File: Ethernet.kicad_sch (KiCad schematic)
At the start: 22 parts, among them J1 PoE, J2301 X05ADGWA3DY1027, U2301 RCLAMP0524P, U2302 RCLAMP0524P

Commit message: Reannotate the board
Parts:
- renumbered C2301 to C71, C2302 to C72, C2303 to C73, C2304 to C74, C2305 to C75, C2306 to C76, C2307 to C77, C2308 to C78, C2309 to C79, D2301 to D20, D2302 to D21, J2301 to J19, J1 to J20, R2301 to R58, R2302 to R59, R2303 to R60, R2304 to R61, R2305 to R62, R2306 to R63, TR2301 to TR1, U2301 to U28, U2302 to U29
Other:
- moved on the sheet: C77

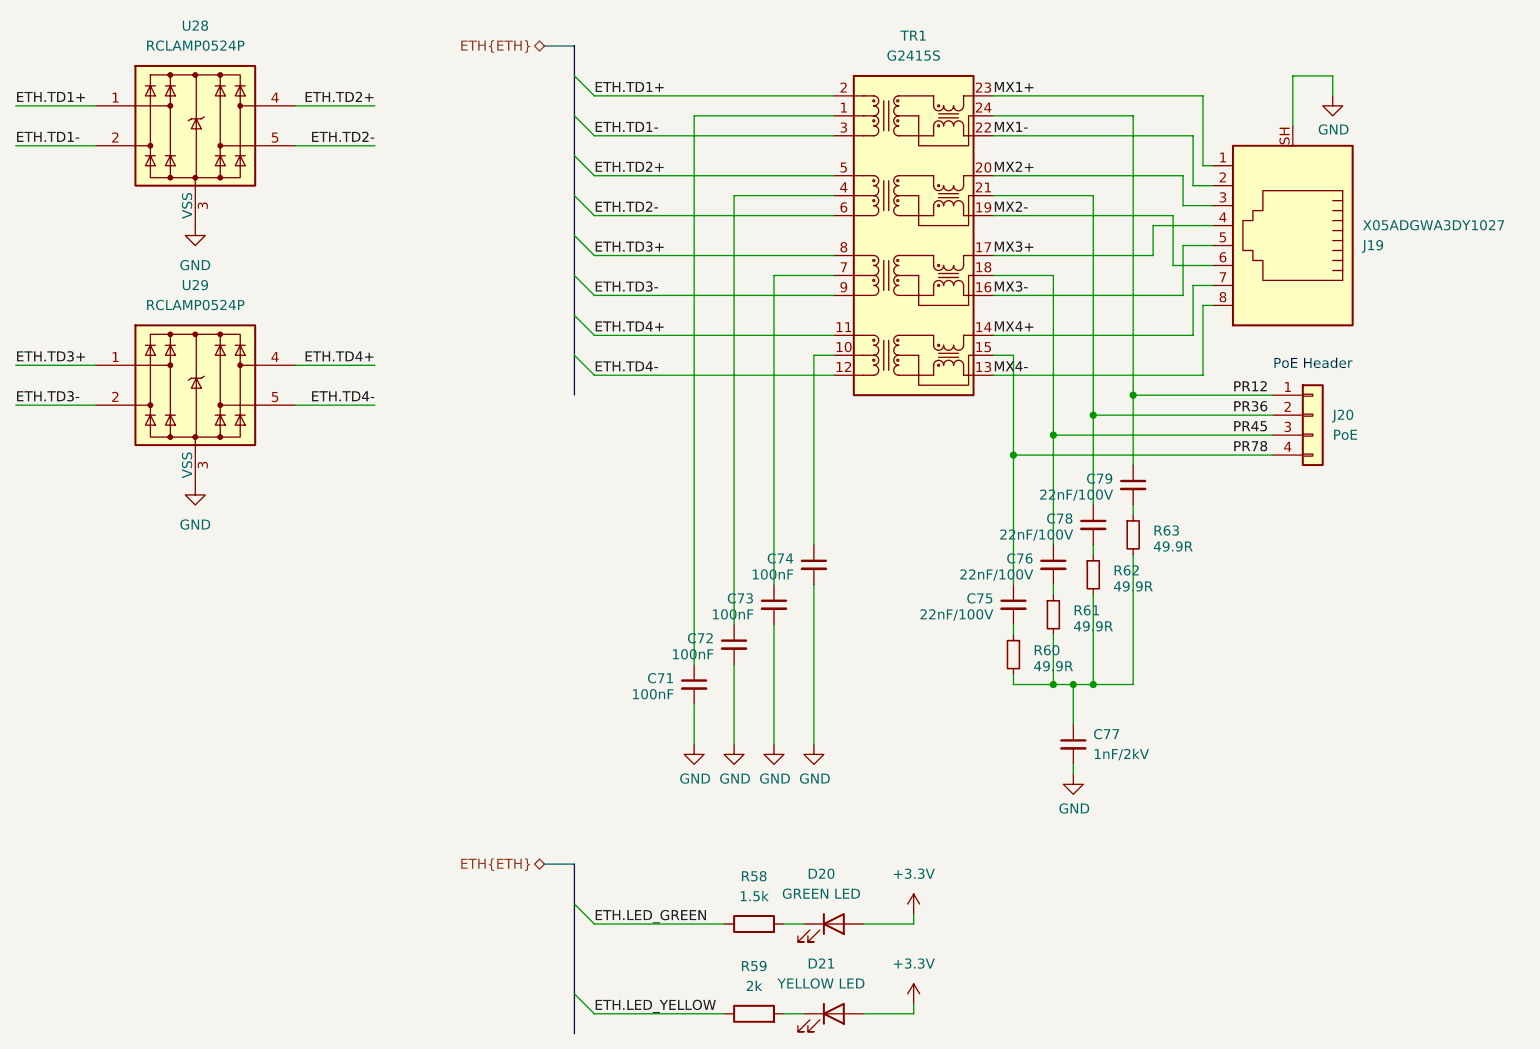
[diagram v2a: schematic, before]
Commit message: Add GND/3.3V/5V headers, add missing JLC part numbers
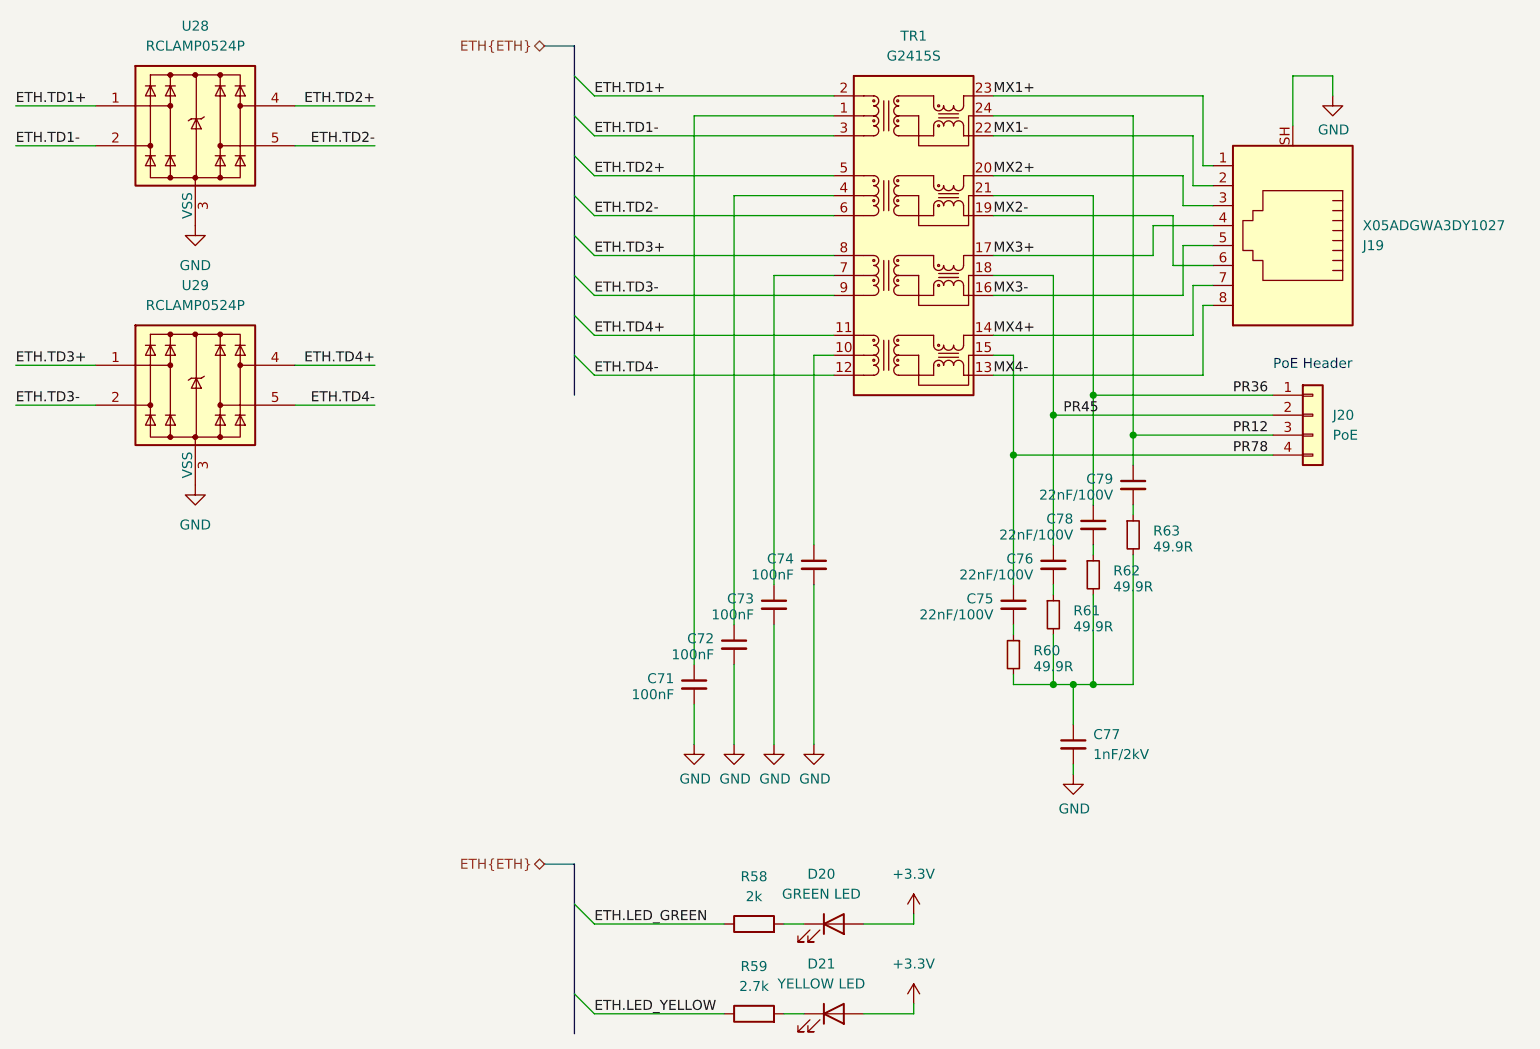
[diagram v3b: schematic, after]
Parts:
- J20: footprint Connector_PinSocket_2.54mm:PinSocket_1x04_P2.54mm_Vertical_SMD_Pin1Left -> Connector_PinSocket_2.54mm:PinSocket_2x02_P2.54mm_Vertical_SMD; LCSC (none) -> C5160817
- R58: value 1.5k -> 2k; footprint Resistor_SMD:R_0402_1005Metric -> Resistor_SMD:R_0603_1608Metric; LCSC C25867 -> C22975
- R59: value 2k -> 2.7k; footprint Resistor_SMD:R_0402_1005Metric -> Resistor_SMD:R_0603_1608Metric; LCSC C4109 -> C13167
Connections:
- net PR12: now also J20.3 (Pin_3); no longer J20.1 (Pin_1)
- net PR36: now also J20.1 (Pin_1); no longer J20.2 (Pin_2)
- net PR45: now also J20.2 (Pin_2); no longer J20.3 (Pin_3)
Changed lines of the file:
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@@
 	)
 	(junction
-		(at 154.94 95.25)
-		(diameter 0)
-		(color 0 0 0 0)
-	)
-	(junction
 		(at 160.02 127)
 		(diameter 0)
@@
 	)
 	(junction
-		(at 160.02 92.71)
+		(at 165.1 95.25)
 		(diameter 0)
 		(color 0 0 0 0)
@@
 	)
 	(junction
-		(at 165.1 90.17)
+		(at 160.02 90.17)
 		(diameter 0)
 		(color 0 0 0 0)
@@
 		(color 0 0 0 0)
 	)
+	(junction
+		(at 154.94 92.71)
+		(diameter 0)
+		(color 0 0 0 0)
+	)
 	(bus_entry
 		(at 93.98 49.53)
@@
 	(wire
 		(pts
-			(xy 165.1 54.61) (xy 165.1 90.17)
-		)
-		(stroke
-			(width 0)
-			(type default)
-		)
-	)
-	(wire
-		(pts
 			(xy 147.32 82.55) (xy 172.72 82.55)
 		)
@@
 	(wire
 		(pts
-			(xy 154.94 74.93) (xy 154.94 95.25)
-		)
-		(stroke
-			(width 0)
-			(type default)
-		)
-	)
-	(wire
-		(pts
 			(xy 171.45 77.47) (xy 147.32 77.47)
 		)
@@
 		)
 	)
+	(wire
+		(pts
+			(xy 154.94 92.71) (xy 154.94 109.22)
+		)
+		(stroke
+			(width 0)
+			(type default)
+		)
+	)
 	(bus
 		(pts
@@
 	(wire
 		(pts
-			(xy 182.88 90.17) (xy 165.1 90.17)
+			(xy 182.88 95.25) (xy 165.1 95.25)
 		)
 		(stroke
@@
 	(wire
 		(pts
-			(xy 160.02 64.77) (xy 160.02 92.71)
+			(xy 160.02 64.77) (xy 160.02 90.17)
 		)
 		(stroke
@@
 	(wire
 		(pts
-			(xy 165.1 90.17) (xy 165.1 99.06)
+			(xy 165.1 54.61) (xy 165.1 95.25)
 		)
 		(stroke
@@
 	(wire
 		(pts
-			(xy 154.94 95.25) (xy 182.88 95.25)
+			(xy 154.94 92.71) (xy 182.88 92.71)
 		)
 		(stroke
@@
 	(wire
 		(pts
-			(xy 160.02 92.71) (xy 160.02 104.14)
+			(xy 160.02 90.17) (xy 160.02 104.14)
 		)
 		(stroke
@@
 	(wire
 		(pts
+			(xy 154.94 74.93) (xy 154.94 92.71)
+		)
+		(stroke
+			(width 0)
+			(type default)
+		)
+	)
+	(wire
+		(pts
 			(xy 175.26 63.5) (xy 172.72 63.5)
 		)
@@
 	(wire
 		(pts
-			(xy 160.02 92.71) (xy 182.88 92.71)
+			(xy 165.1 95.25) (xy 165.1 99.06)
+		)
+		(stroke
+			(width 0)
+			(type default)
+		)
+	)
+	(wire
+		(pts
+			(xy 160.02 90.17) (xy 182.88 90.17)
 		)
 		(stroke
@@
 	(wire
 		(pts
-			(xy 154.94 109.22) (xy 154.94 95.25)
-		)
-		(stroke
-			(width 0)
-			(type default)
-		)
-	)
-	(wire
-		(pts
 			(xy 157.48 138.43) (xy 157.48 137.16)
 		)
@@
 	)
 	(label "PR36"
-		(at 177.8 92.71 0)
+		(at 177.8 90.17 0)
 		(effects
 			(font
@@
 	)
 	(label "PR45"
-		(at 177.8 95.25 0)
+		(at 156.21 92.71 0)
 		(effects
 			(font
@@
 	)
 	(label "PR12"
-		(at 177.8 90.17 0)
+		(at 177.8 95.25 0)
 		(effects
 			(font
@@
 			)
 		)
-		(property "Value" "2k"
+		(property "Value" "2.7k"
 			(at 116.84 165.4175 90)
 			(effects
@@
 			)
 		)
-		(property "Footprint" "Resistor_SMD:R_0402_1005Metric"
+		(property "Footprint" "Resistor_SMD:R_0603_1608Metric"
 			(at 116.84 170.688 90)
 			(effects
@@
 			)
 		)
-		(property "LCSC" "C4109"
+		(property "LCSC" "C13167"
 			(at 116.84 168.91 0)
 			(effects
@@
 			)
 		)
-		(property "Field8" ""
-			(at 116.84 168.91 0)
-			(effects
-				(font
-					(size 1.27 1.27)
-				)
-			)
-		)
 		(property "PartNumber" ""
 			(at 116.84 168.91 0)
@@
 			)
 		)
-		(property "Value" "1.5k"
+		(property "Value" "2k"
 			(at 116.84 153.9875 90)
 			(effects
@@
 			)
 		)
-		(property "Footprint" "Resistor_SMD:R_0402_1005Metric"
+		(property "Footprint" "Resistor_SMD:R_0603_1608Metric"
 			(at 116.84 159.258 90)
 			(effects
@@
 			)
 		)
-		(property "LCSC" "C25867"
+		(property "LCSC" "C22975"
 			(at 116.84 157.48 0)
 			(effects
@@
 			)
 		)
-		(property "Field8" ""
-			(at 116.84 157.48 0)
-			(effects
-				(font
-					(size 1.27 1.27)
-				)
-			)
-		)
 		(property "PartNumber" ""
 			(at 116.84 157.48 0)
@@
 			)
 		)
-		(property "Footprint" "Connector_PinSocket_2.54mm:PinSocket_1x04_P2.54mm_Vertical_SMD_Pin1Left"
+		(property "Footprint" "Connector_PinSocket_2.54mm:PinSocket_2x02_P2.54mm_Vertical_SMD"
 			(at 187.96 92.71 0)
 			(effects
@@
 			)
 		)
-		(property "Field8" ""
+		(property "PartNumber" ""
 			(at 187.96 92.71 0)
 			(effects
@@
 			)
 		)
-		(property "PartNumber" ""
+		(property "Sim.Enable" ""
 			(at 187.96 92.71 0)
 			(effects
@@
 			)
 		)
-		(property "Sim.Enable" ""
+		(property "LCSC" "C5160817"
 			(at 187.96 92.71 0)
 			(effects
@@
 					(size 1.27 1.27)
 				)
+				(hide yes)
 			)
 		)

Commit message: FInal v0.2.0 proto changes
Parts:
- J20: JLCPCB_CORRECTION (none) -> 0;0;90
- renumbered C71 to C73, C72 to C74, C73 to C75, C74 to C76, C75 to C77, C76 to C78, C77 to C79, C78 to C80, C79 to C81
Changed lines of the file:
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@@
 		(polyline
 			(pts
-				(xy 125.73 104.14) (xy 107.95 104.14) (xy 107.95 101.6) (xy 125.73 101.6)
+				(xy 167.64 43.18) (xy 167.64 134.62) (xy 133.35 134.62) (xy 133.35 43.18)
 			)
 			(stroke
@@
 		(polyline
 			(pts
-				(xy 167.64 43.18) (xy 167.64 134.62) (xy 133.35 134.62) (xy 133.35 43.18)
+				(xy 175.26 88.9) (xy 175.26 99.06) (xy 172.72 99.06) (xy 172.72 88.9)
 			)
 			(stroke
@@
 		(polyline
 			(pts
-				(xy 175.26 88.9) (xy 175.26 99.06) (xy 172.72 99.06) (xy 172.72 88.9)
+				(xy 125.73 104.14) (xy 107.95 104.14) (xy 107.95 101.6) (xy 125.73 101.6)
 			)
 			(stroke
@@
 		(dnp no)
 		(fields_autoplaced yes)
-		(property "Reference" "C77"
+		(property "Reference" "C79"
 			(at 160.02 133.3562 0)
 			(effects
@@
 			(project "HALPI2"
 				(path "/abc482bd-3f17-4d35-80db-1da3dcdb5c27/18c18357-12fa-4472-a108-e954e5bd7840"
-					(reference "C77")
+					(reference "C79")
 					(unit 1)
 				)
@@
 		(on_board yes)
 		(dnp no)
-		(property "Reference" "#PWR0158"
+		(property "Reference" "#PWR0159"
 			(at 157.48 144.78 0)
 			(effects
@@
 			(project "HALPI2"
 				(path "/abc482bd-3f17-4d35-80db-1da3dcdb5c27/18c18357-12fa-4472-a108-e954e5bd7840"
-					(reference "#PWR0158")
+					(reference "#PWR0159")
 					(unit 1)
 				)
@@
 		(on_board yes)
 		(dnp no)
-		(property "Reference" "C74"
+		(property "Reference" "C76"
 			(at 121.92 110.998 0)
 			(effects
@@
 			(project "HALPI2"
 				(path "/abc482bd-3f17-4d35-80db-1da3dcdb5c27/18c18357-12fa-4472-a108-e954e5bd7840"
-					(reference "C74")
+					(reference "C76")
 					(unit 1)
 				)
@@
 		(on_board yes)
 		(dnp no)
-		(property "Reference" "C79"
+		(property "Reference" "C81"
 			(at 162.56 100.838 0)
 			(effects
@@
 			(project "HALPI2"
 				(path "/abc482bd-3f17-4d35-80db-1da3dcdb5c27/18c18357-12fa-4472-a108-e954e5bd7840"
-					(reference "C79")
+					(reference "C81")
 					(unit 1)
 				)
@@
 		(on_board yes)
 		(dnp no)
-		(property "Reference" "C76"
+		(property "Reference" "C78"
 			(at 152.4 110.998 0)
 			(effects
@@
 			(project "HALPI2"
 				(path "/abc482bd-3f17-4d35-80db-1da3dcdb5c27/18c18357-12fa-4472-a108-e954e5bd7840"
-					(reference "C76")
+					(reference "C78")
 					(unit 1)
 				)
@@
 		(on_board yes)
 		(dnp no)
-		(property "Reference" "C75"
+		(property "Reference" "C77"
 			(at 147.32 116.078 0)
 			(effects
@@
 			(project "HALPI2"
 				(path "/abc482bd-3f17-4d35-80db-1da3dcdb5c27/18c18357-12fa-4472-a108-e954e5bd7840"
-					(reference "C75")
+					(reference "C77")
 					(unit 1)
 				)
@@
 		(dnp no)
 		(fields_autoplaced yes)
-		(property "Reference" "#PWR0150"
+		(property "Reference" "#PWR0151"
 			(at 45.72 74.93 0)
 			(effects
@@
 			(project "Yellow"
 				(path "/abc482bd-3f17-4d35-80db-1da3dcdb5c27/18c18357-12fa-4472-a108-e954e5bd7840"
-					(reference "#PWR0150")
+					(reference "#PWR0151")
 					(unit 1)
 				)
@@
 		(dnp no)
 		(fields_autoplaced yes)
-		(property "Reference" "#PWR0156"
+		(property "Reference" "#PWR0157"
 			(at 137.16 160.02 0)
 			(effects
@@
 			(project ""
 				(path "/abc482bd-3f17-4d35-80db-1da3dcdb5c27/18c18357-12fa-4472-a108-e954e5bd7840"
-					(reference "#PWR0156")
+					(reference "#PWR0157")
 					(unit 1)
 				)
@@
 		(on_board yes)
 		(dnp no)
-		(property "Reference" "#PWR0159"
+		(property "Reference" "#PWR0160"
 			(at 190.5 58.42 0)
 			(effects
@@
 			(project "HALPI2"
 				(path "/abc482bd-3f17-4d35-80db-1da3dcdb5c27/18c18357-12fa-4472-a108-e954e5bd7840"
-					(reference "#PWR0159")
+					(reference "#PWR0160")
 					(unit 1)
 				)
@@
 		(on_board yes)
 		(dnp no)
-		(property "Reference" "C71"
+		(property "Reference" "C73"
 			(at 106.68 126.238 0)
 			(effects
@@
 			(project "HALPI2"
 				(path "/abc482bd-3f17-4d35-80db-1da3dcdb5c27/18c18357-12fa-4472-a108-e954e5bd7840"
-					(reference "C71")
+					(reference "C73")
 					(unit 1)
 				)
@@
 		(on_board yes)
 		(dnp no)
-		(property "Reference" "C73"
+		(property "Reference" "C75"
 			(at 116.84 116.078 0)
 			(effects
@@
 			(project "HALPI2"
 				(path "/abc482bd-3f17-4d35-80db-1da3dcdb5c27/18c18357-12fa-4472-a108-e954e5bd7840"
-					(reference "C73")
+					(reference "C75")
 					(unit 1)
 				)
@@
 		(dnp no)
 		(fields_autoplaced yes)
-		(property "Reference" "#PWR0151"
+		(property "Reference" "#PWR0152"
 			(at 45.72 107.95 0)
 			(effects
@@
 			(project "Yellow"
 				(path "/abc482bd-3f17-4d35-80db-1da3dcdb5c27/18c18357-12fa-4472-a108-e954e5bd7840"
-					(reference "#PWR0151")
+					(reference "#PWR0152")
 					(unit 1)
 				)
@@
 		(dnp no)
 		(fields_autoplaced yes)
-		(property "Reference" "#PWR0157"
+		(property "Reference" "#PWR0158"
 			(at 137.16 171.45 0)
 			(effects
@@
 			(project "HALPI2"
 				(path "/abc482bd-3f17-4d35-80db-1da3dcdb5c27/18c18357-12fa-4472-a108-e954e5bd7840"
-					(reference "#PWR0157")
+					(reference "#PWR0158")
 					(unit 1)
 				)
@@
 			)
 		)
-		(property "Sim.Enable" ""
+		(property "LCSC" "C5160817"
 			(at 187.96 92.71 0)
 			(effects
@@
 					(size 1.27 1.27)
 				)
+				(hide yes)
 			)
 		)
-		(property "LCSC" "C5160817"
+		(property "JLCPCB_CORRECTION" "0;0;90"
+			(at 187.96 92.71 0)
+			(effects
+				(font
+					(size 1.27 1.27)
+				)
+			)
+		)
+		(property "Sim.Enable" ""
 			(at 187.96 92.71 0)
 			(effects
@@
 					(size 1.27 1.27)
 				)
-				(hide yes)
 			)
 		)
@@
 		(on_board yes)
 		(dnp no)
-		(property "Reference" "#PWR0154"
+		(property "Reference" "#PWR0155"
 			(at 119.38 140.97 0)
 			(effects
@@
 			(project "HALPI2"
 				(path "/abc482bd-3f17-4d35-80db-1da3dcdb5c27/18c18357-12fa-4472-a108-e954e5bd7840"
-					(reference "#PWR0154")
+					(reference "#PWR0155")
 					(unit 1)
 				)
@@
 		(on_board yes)
 		(dnp no)
-		(property "Reference" "#PWR0153"
+		(property "Reference" "#PWR0154"
 			(at 114.3 140.97 0)
 			(effects
@@
 			(project "HALPI2"
 				(path "/abc482bd-3f17-4d35-80db-1da3dcdb5c27/18c18357-12fa-4472-a108-e954e5bd7840"
-					(reference "#PWR0153")
+					(reference "#PWR0154")
 					(unit 1)
 				)
@@
 		(on_board yes)
 		(dnp no)
-		(property "Reference" "C78"
+		(property "Reference" "C80"
 			(at 157.48 105.918 0)
 			(effects
@@
 			(project "HALPI2"
 				(path "/abc482bd-3f17-4d35-80db-1da3dcdb5c27/18c18357-12fa-4472-a108-e954e5bd7840"
-					(reference "C78")
+					(reference "C80")
 					(unit 1)
 				)
@@
 		(on_board yes)
 		(dnp no)
-		(property "Reference" "#PWR0155"
+		(property "Reference" "#PWR0156"
 			(at 124.46 140.97 0)
 			(effects
@@
 			(project "HALPI2"
 				(path "/abc482bd-3f17-4d35-80db-1da3dcdb5c27/18c18357-12fa-4472-a108-e954e5bd7840"
-					(reference "#PWR0155")
+					(reference "#PWR0156")
 					(unit 1)
 				)
@@
 		(on_board yes)
 		(dnp no)
-		(property "Reference" "C72"
+		(property "Reference" "C74"
 			(at 111.76 121.158 0)
 			(effects
@@
 			(project "HALPI2"
 				(path "/abc482bd-3f17-4d35-80db-1da3dcdb5c27/18c18357-12fa-4472-a108-e954e5bd7840"
-					(reference "C72")
+					(reference "C74")
 					(unit 1)
 				)
@@
 		(on_board yes)
 		(dnp no)
-		(property "Reference" "#PWR0152"
+		(property "Reference" "#PWR0153"
 			(at 109.22 140.97 0)
 			(effects
@@
 			(project "HALPI2"
 				(path "/abc482bd-3f17-4d35-80db-1da3dcdb5c27/18c18357-12fa-4472-a108-e954e5bd7840"
-					(reference "#PWR0152")
+					(reference "#PWR0153")
 					(unit 1)
 				)

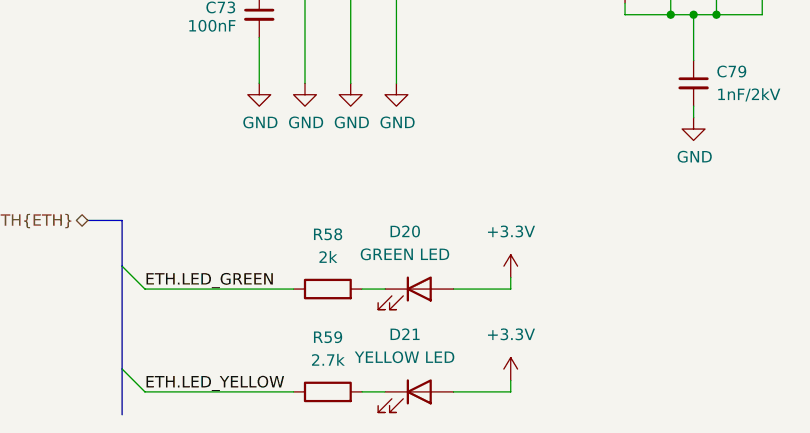
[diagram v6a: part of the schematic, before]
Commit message: Nailed the current limiter design
Also added more GND test pads
Also fixed the MCU I2C pinout
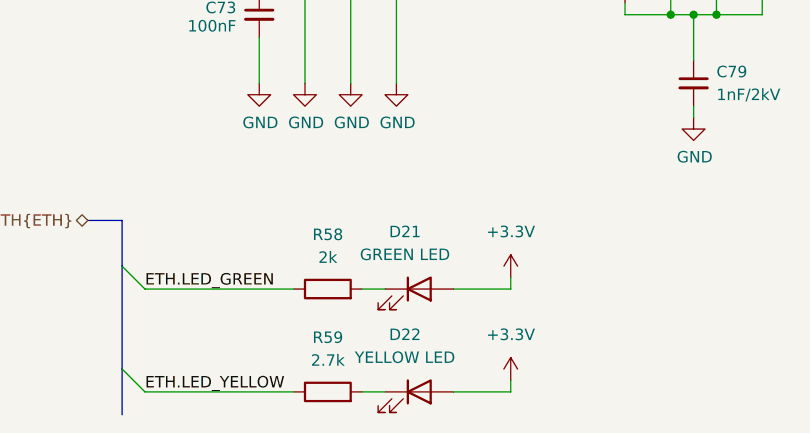
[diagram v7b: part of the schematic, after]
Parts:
- renumbered D20 to D21, D21 to D22
